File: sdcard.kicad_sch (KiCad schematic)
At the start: 0 parts

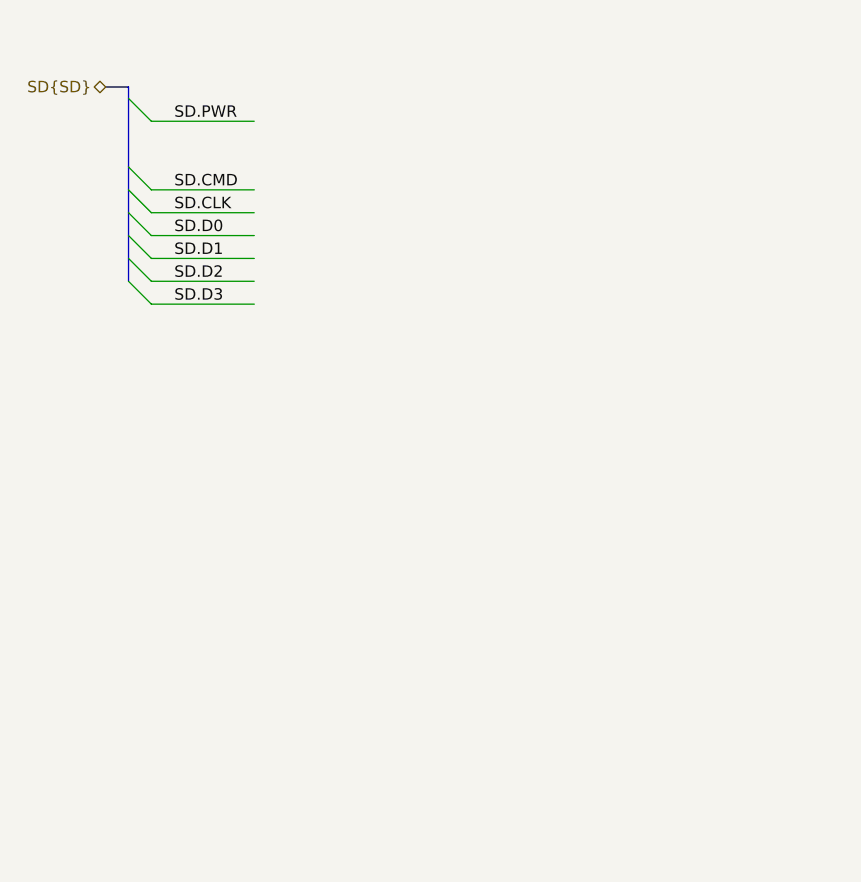
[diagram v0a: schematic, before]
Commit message: Wired up SD card
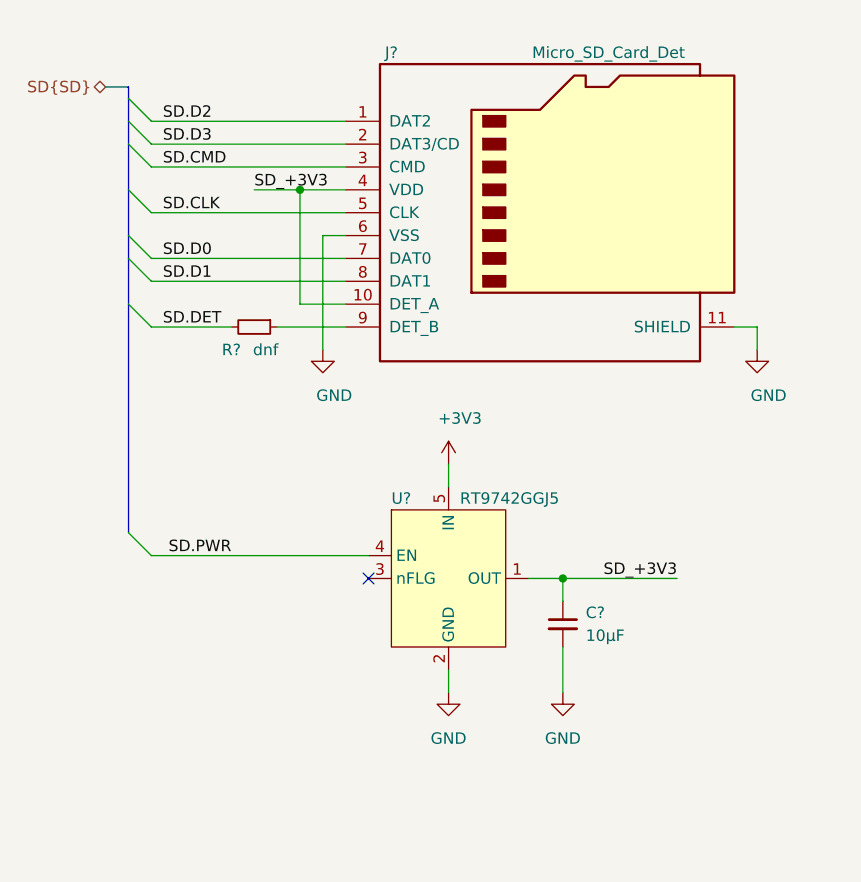
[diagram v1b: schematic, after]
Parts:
- added C?: 10μF, symbol Device:C_Small
- added J?: Micro_SD_Card_Det, Connector_Card:microSD_HC_Molex_104031-0811, symbol Connector:Micro_SD_Card_Det
- added R?: dnf, symbol Device:R_Small
- added U?: RT9742GGJ5, Package_TO_SOT_SMD:SOT-23-5, symbol LightBlue:RT9742GGJ5
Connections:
- net SD.CLK: now also J?.5 (CLK)
- net SD.CMD: now also J?.3 (CMD)
- net SD.D0: now also J?.7 (DAT0)
- net SD.D1: now also J?.8 (DAT1)
- net SD.D2: now also J?.1 (DAT2)
- net SD.D3: now also J?.2 (DAT3/CD)
- net SD.PWR: now also U?.4 (EN)
- new net: J?.9 (DET_B), R?.1
- new net +3V3: U?.5 (IN)
- new net GND: C?.2, J?.11 (SHIELD), J?.6 (VSS), U?.2 (GND)
- new net SD.DET: R?.2
- new net SD_+3V3: C?.1, J?.10 (DET_A), J?.4 (VDD), U?.1 (OUT)
- no-connect marks 0 -> 1

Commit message: -Connected remaining nets -CM4 symbol fixups -Used single 6x OE buffer chip instead of 4x single -Added PWM FAN
Signed-off-by: Dominik Sliwa <dominik@sliwa.io>
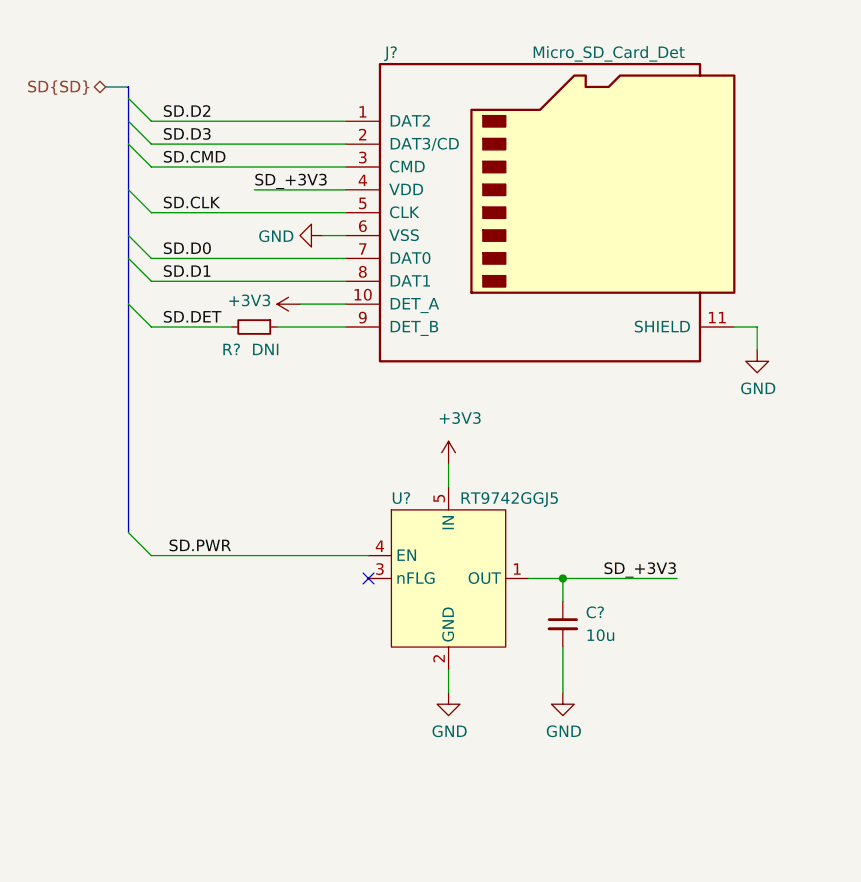
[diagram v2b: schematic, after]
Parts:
- C?: value 10μF -> 10u
- R?: value dnf -> DNI
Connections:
- net +3V3: now also J?.10 (DET_A)
- net SD_+3V3: no longer J?.10 (DET_A)
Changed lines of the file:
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@@
 (kicad_sch (version 20201015) (generator eeschema)
   (paper "A4")
-  (junction (at 67.31 54.61) (diameter 0.9144) (color 0 0 0 0))
   (junction (at 96.52 97.79) (diameter 0.9144) (color 0 0 0 0))
   (no_connect (at 74.93 97.79))
@@
     (stroke (width 0) (type solid) (color 0 0 0 0))
   )
-  (wire (pts (xy 62.23 54.61) (xy 67.31 54.61))
+  (wire (pts (xy 62.23 54.61) (xy 72.39 54.61))
     (stroke (width 0) (type solid) (color 0 0 0 0))
   )
@@
     (stroke (width 0) (type solid) (color 0 0 0 0))
   )
-  (wire (pts (xy 67.31 54.61) (xy 67.31 67.31))
-    (stroke (width 0) (type solid) (color 0 0 0 0))
-  )
-  (wire (pts (xy 67.31 54.61) (xy 72.39 54.61))
-    (stroke (width 0) (type solid) (color 0 0 0 0))
-  )
   (wire (pts (xy 67.31 67.31) (xy 72.39 67.31))
-    (stroke (width 0) (type solid) (color 0 0 0 0))
-  )
-  (wire (pts (xy 69.85 59.69) (xy 69.85 72.39))
     (stroke (width 0) (type solid) (color 0 0 0 0))
   )
@@
     (effects (font (size 1.27 1.27)) (justify right))
   )
+  (symbol (lib_id "power:+3V3") (at 67.31 67.31 90) (unit 1)
+    (in_bom yes) (on_board yes)
+    (property "Reference" "#PWR?" (id 0) (at 71.12 67.31 0)
+      (effects (font (size 1.27 1.27)) hide)
+    )
+    (property "Value" "+3V3" (id 1) (at 64.1349 66.9417 90)
+      (effects (font (size 1.27 1.27)) (justify left))
+    )
+    (property "Footprint" "" (id 2) (at 67.31 67.31 0)
+      (effects (font (size 1.27 1.27)) hide)
+    )
+    (property "Datasheet" "" (id 3) (at 67.31 67.31 0)
+      (effects (font (size 1.27 1.27)) hide)
+    )
+  )
   (symbol (lib_id "power:+3V3") (at 83.82 85.09 0) (unit 1)
     (in_bom yes) (on_board yes)
@@
     )
   )
-  (symbol (lib_id "power:GND") (at 69.85 72.39 0) (unit 1)
-    (in_bom yes) (on_board yes)
-    (property "Reference" "#PWR?" (id 0) (at 69.85 78.74 0)
-      (effects (font (size 1.27 1.27)) hide)
-    )
-    (property "Value" "GND" (id 1) (at 71.12 77.47 0))
-    (property "Footprint" "" (id 2) (at 69.85 72.39 0)
-      (effects (font (size 1.27 1.27)) hide)
-    )
-    (property "Datasheet" "" (id 3) (at 69.85 72.39 0)
+  (symbol (lib_id "power:GND") (at 69.85 59.69 270) (unit 1)
+    (in_bom yes) (on_board yes)
+    (property "Reference" "#PWR?" (id 0) (at 63.5 59.69 0)
+      (effects (font (size 1.27 1.27)) hide)
+    )
+    (property "Value" "GND" (id 1) (at 66.675 59.8043 90)
+      (effects (font (size 1.27 1.27)) (justify right))
+    )
+    (property "Footprint" "" (id 2) (at 69.85 59.69 0)
+      (effects (font (size 1.27 1.27)) hide)
+    )
+    (property "Datasheet" "" (id 3) (at 69.85 59.69 0)
       (effects (font (size 1.27 1.27)) hide)
     )
@@
       (effects (font (size 1.27 1.27)) hide)
     )
-    (property "Value" "GND" (id 1) (at 83.82 115.57 0))
+    (property "Value" "GND" (id 1) (at 83.9343 114.8144 0))
     (property "Footprint" "" (id 2) (at 83.82 110.49 0)
       (effects (font (size 1.27 1.27)) hide)
@@
       (effects (font (size 1.27 1.27)) hide)
     )
-    (property "Value" "GND" (id 1) (at 96.52 115.57 0))
+    (property "Value" "GND" (id 1) (at 96.6343 114.8144 0))
     (property "Footprint" "" (id 2) (at 96.52 110.49 0)
       (effects (font (size 1.27 1.27)) hide)
@@
       (effects (font (size 1.27 1.27)) hide)
     )
-    (property "Value" "GND" (id 1) (at 119.38 77.47 0))
+    (property "Value" "GND" (id 1) (at 118.2243 76.7144 0))
     (property "Footprint" "" (id 2) (at 118.11 72.39 0)
       (effects (font (size 1.27 1.27)) hide)
@@
     (in_bom yes) (on_board yes)
     (property "Reference" "R?" (id 0) (at 59.69 72.39 90))
-    (property "Value" "dnf" (id 1) (at 63.5 72.39 90))
+    (property "Value" "DNI" (id 1) (at 63.5 72.39 90))
     (property "Footprint" "" (id 2) (at 62.23 69.85 0)
       (effects (font (size 1.27 1.27)) hide)
@@
       (effects (font (size 1.27 1.27)) (justify left))
     )
-    (property "Value" "10μF" (id 1) (at 99.06 104.14 0)
+    (property "Value" "10u" (id 1) (at 99.06 104.14 0)
       (effects (font (size 1.27 1.27)) (justify left))
     )

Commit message: PoE and clean-up
- Moved PoE to a seperate sheet and finished design
- Started using Config field for Variants and DNP flag
- Fix-ups
- Added Wurth 749119550 and TI TPS23734 to the symbol library
- Changed RTC from PCF8563 to PCF85063

Signed-off-by: Dominik Sliwa <dominik@sliwa.io>
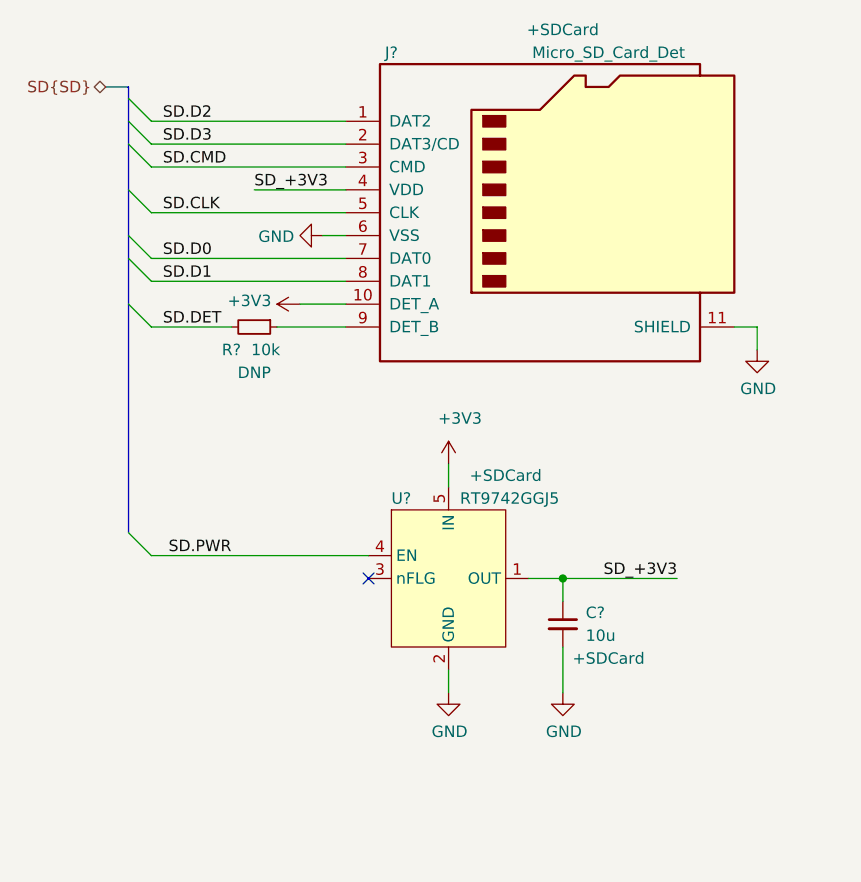
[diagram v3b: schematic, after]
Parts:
- C?, J?, U?: Config (none) -> +SDCard
- R?: value DNI -> 10k; Config (none) -> DNP
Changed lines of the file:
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@@
     (in_bom yes) (on_board yes)
     (property "Reference" "R?" (id 0) (at 59.69 72.39 90))
-    (property "Value" "DNI" (id 1) (at 63.5 72.39 90))
+    (property "Value" "10k" (id 1) (at 63.5 72.39 90))
     (property "Footprint" "" (id 2) (at 62.23 69.85 0)
       (effects (font (size 1.27 1.27)) hide)
@@
       (effects (font (size 1.27 1.27)) hide)
     )
+    (property "Config" "DNP" (id 4) (at 62.23 74.93 90))
   )
   (symbol (lib_id "Device:C_Small") (at 96.52 102.87 0) (unit 1)
@@
       (effects (font (size 1.27 1.27)) hide)
     )
+    (property "Config" "+SDCard" (id 4) (at 101.6 106.68 0))
   )
   (symbol (lib_id "LightBlue:RT9742GGJ5") (at 83.82 97.79 0) (unit 1)
@@
       (effects (font (size 1.27 1.27)) hide)
     )
+    (property "Config" "+SDCard" (id 4) (at 90.17 86.36 0))
   )
   (symbol (lib_id "Connector:Micro_SD_Card_Det") (at 95.25 57.15 0) (unit 1)
@@
       (effects (font (size 1.27 1.27)) hide)
     )
+    (property "Config" "+SDCard" (id 4) (at 96.52 36.83 0))
   )
 )

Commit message: Annotate symbools and assign capacitor footprints
Signed-off-by: Stefan Agner <stefan@agner.ch>
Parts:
- C69: renamed from C?; footprint (none) -> Capacitor_SMD:C_0805_2012Metric
- gave numbers to parts that had none: 3
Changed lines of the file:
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@@
   (symbol (lib_id "Device:R_Small") (at 62.23 69.85 270) (unit 1)
     (in_bom yes) (on_board yes)
-    (property "Reference" "R?" (id 0) (at 59.69 72.39 90))
+    (property "Reference" "R36" (id 0) (at 59.69 72.39 90))
     (property "Value" "10k" (id 1) (at 63.5 72.39 90))
     (property "Footprint" "" (id 2) (at 62.23 69.85 0)
@@
   (symbol (lib_id "Device:C_Small") (at 96.52 102.87 0) (unit 1)
     (in_bom yes) (on_board yes)
-    (property "Reference" "C?" (id 0) (at 99.06 101.6 0)
+    (property "Reference" "C69" (id 0) (at 99.06 101.6 0)
       (effects (font (size 1.27 1.27)) (justify left))
     )
@@
       (effects (font (size 1.27 1.27)) (justify left))
     )
-    (property "Footprint" "" (id 2) (at 96.52 102.87 0)
+    (property "Footprint" "Capacitor_SMD:C_0805_2012Metric" (id 2) (at 96.52 102.87 0)
       (effects (font (size 1.27 1.27)) hide)
     )
@@
   (symbol (lib_id "LightBlue:RT9742GGJ5") (at 83.82 97.79 0) (unit 1)
     (in_bom yes) (on_board yes)
-    (property "Reference" "U?" (id 0) (at 77.47 88.9 0)
+    (property "Reference" "U19" (id 0) (at 77.47 88.9 0)
       (effects (font (size 1.27 1.27)) (justify left))
     )
@@
   (symbol (lib_id "Connector:Micro_SD_Card_Det") (at 95.25 57.15 0) (unit 1)
     (in_bom yes) (on_board yes)
-    (property "Reference" "J?" (id 0) (at 77.47 39.37 0))
+    (property "Reference" "J12" (id 0) (at 77.47 39.37 0))
     (property "Value" "Micro_SD_Card_Det" (id 1) (at 101.6 39.37 0))
     (property "Footprint" "Connector_Card:microSD_HC_Molex_104031-0811" (id 2) (at 147.32 39.37 0)

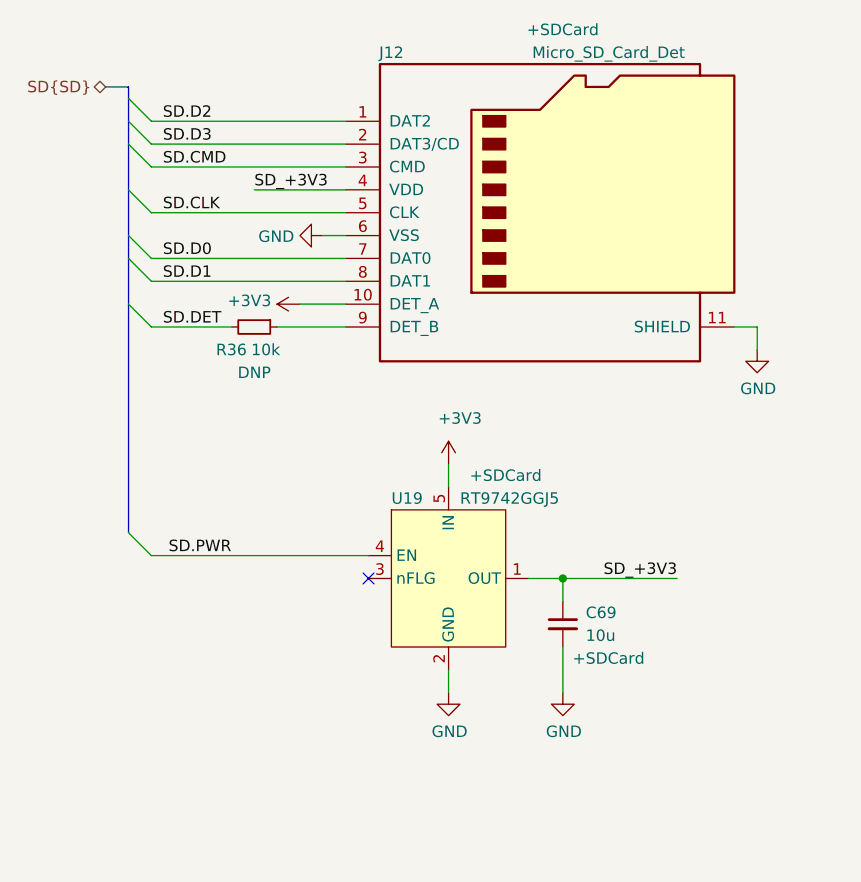
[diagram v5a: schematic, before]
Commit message: Standardize page settings/add page titles
Signed-off-by: Stefan Agner <stefan@agner.ch>
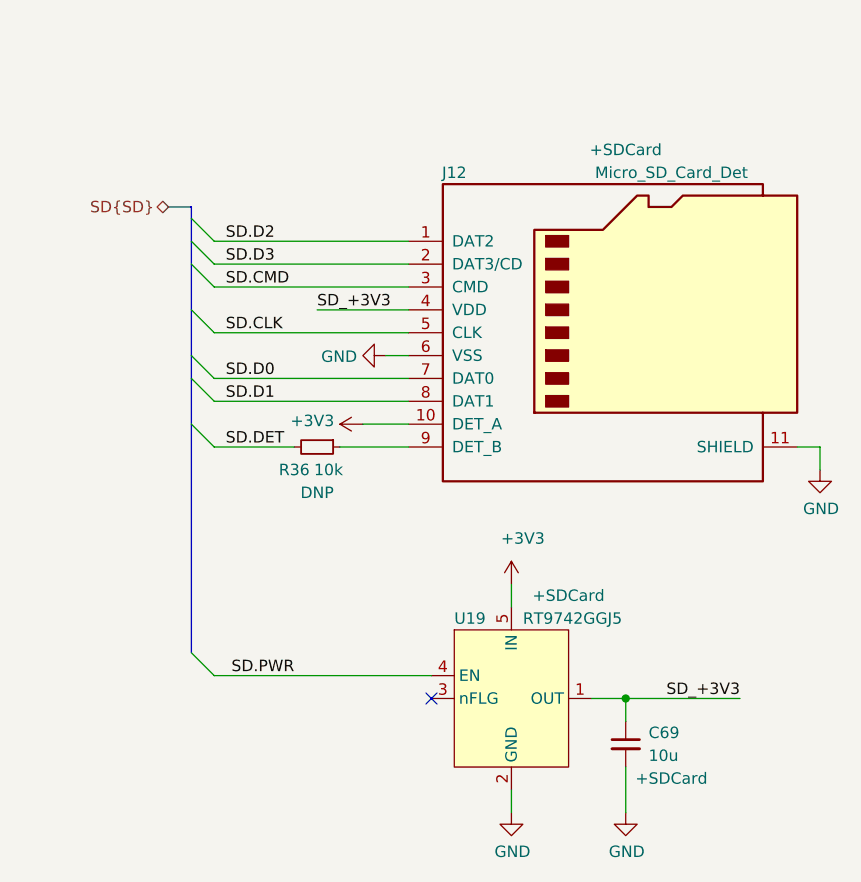
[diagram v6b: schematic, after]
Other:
- company: (none) -> Nabu Casa
- title: (none) -> SD card
- moved on the sheet: C69, J12, R36, U19

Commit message: Define more footprints and update Manufacturer/PartNumber fields
Signed-off-by: Stefan Agner <stefan@agner.ch>
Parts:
- U19: Manufacturer (none) -> Richtek USA; PartNumber (none) -> RT9742GGJ5
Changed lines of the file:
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@@
     )
     (property "Config" "+SDCard" (id 4) (at 97.155 99.695 0))
+    (property "Manufacturer" "Richtek USA" (id 4) (at 90.805 111.125 0)
+      (effects (font (size 1.27 1.27)) hide)
+    )
+    (property "PartNumber" "RT9742GGJ5" (id 5) (at 90.805 111.125 0)
+      (effects (font (size 1.27 1.27)) hide)
+    )
   )
   (symbol (lib_id "Connector:Micro_SD_Card_Det") (at 102.235 70.485 0) (unit 1)
